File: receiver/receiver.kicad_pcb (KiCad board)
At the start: 2 copper layers, 71.4 x 53.5 mm, 53 parts, among them CON1 AVR-ISP-6, IC1 ATTINY441-SSU, P1 LASER, P2 BATTERY, P3 CONN_01X01, P4 CONN_01X01, P5 CONN_01X01, Q1 OPTO_NPN, Q2 OPTO_NPN, Q3 OPTO_NPN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

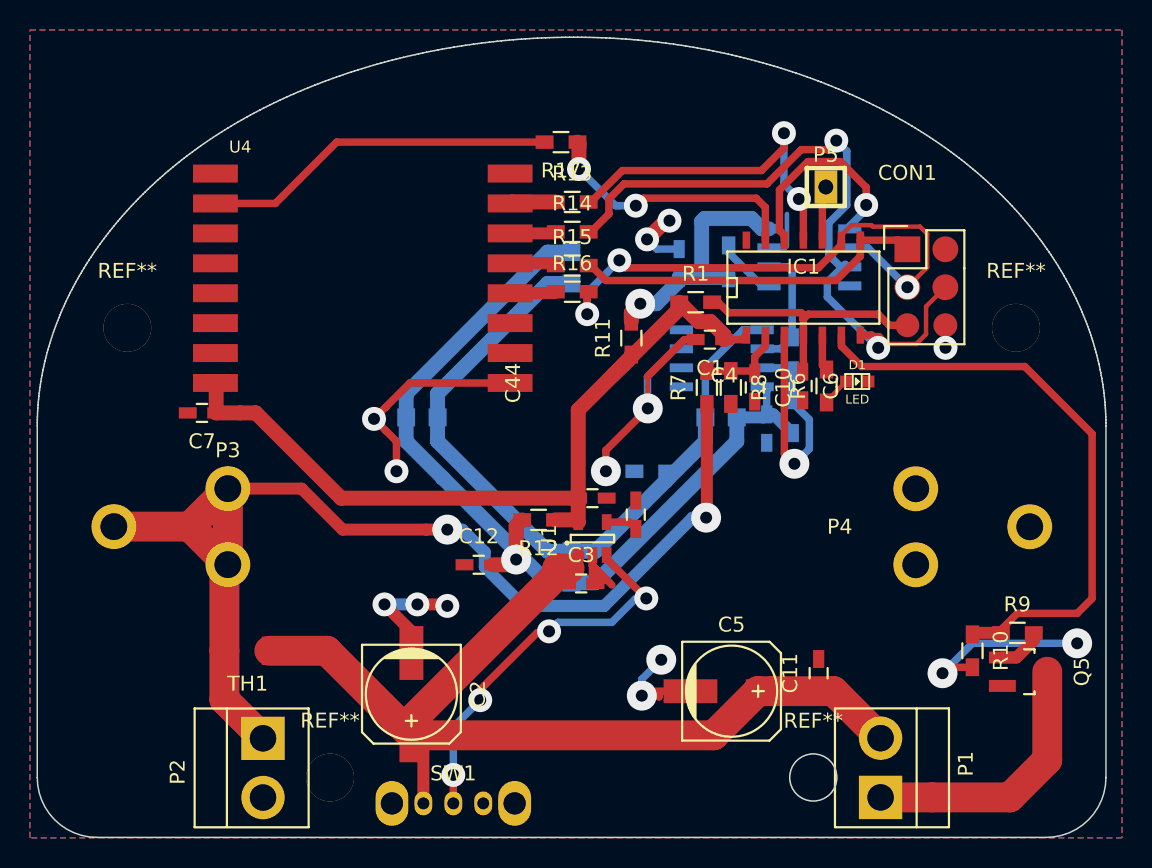
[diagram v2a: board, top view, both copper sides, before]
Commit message: Add connections to the switch on the bottom side
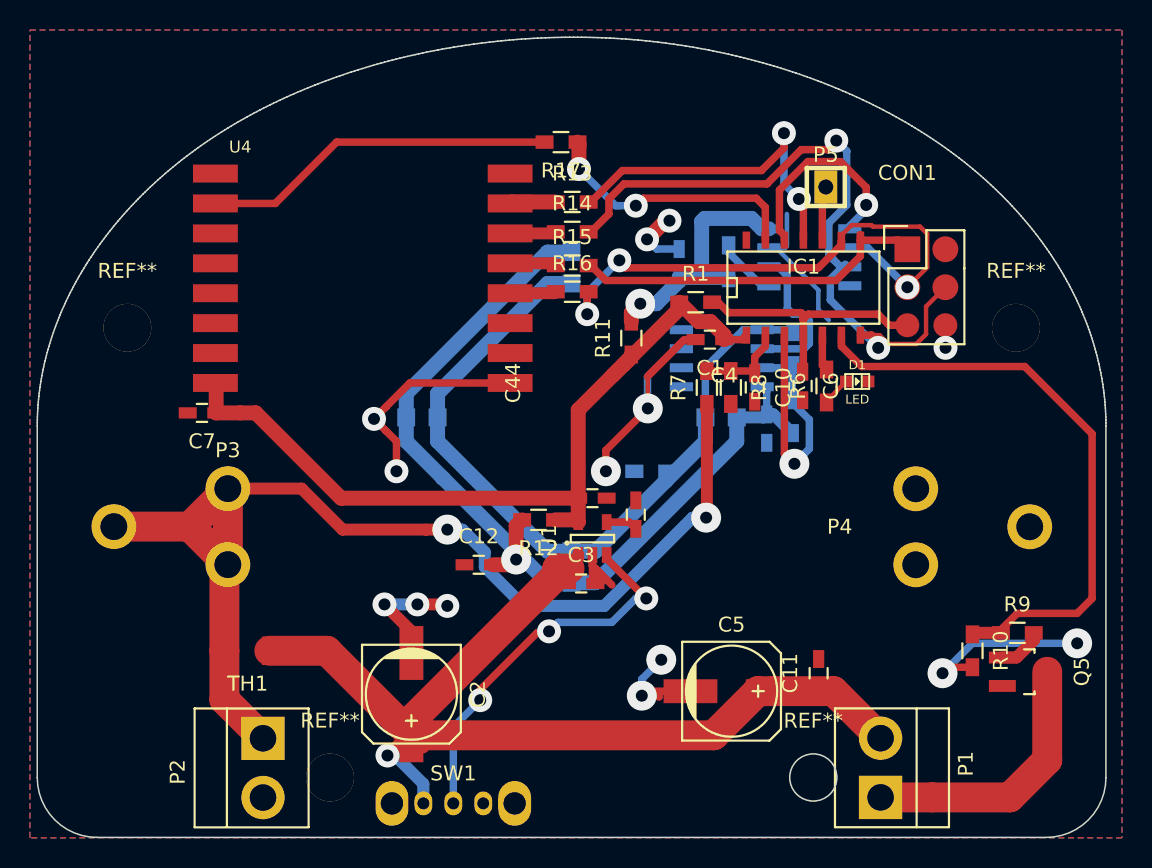
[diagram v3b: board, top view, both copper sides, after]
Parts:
- moved R3 0.35 mm to (102.0, 101.3)
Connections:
- R3 pad 1: /THRESHOLD -> /MATRIX_OUT
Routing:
- net GND: track 76.2 -> 83.0 mm
- net VAA: track 73.1 -> 76.0 mm, vias 0 -> 1
- net /MATRIX_OUT: track 49.7 -> 51.8 mm
- net /THRESHOLD: track 8.51 -> 10.3 mm
- net Net-(SW1-Pad2): vias 4 -> 3
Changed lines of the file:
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@@
     (thickness 1.6)
     (drawings 469)
-    (tracks 393)
+    (tracks 405)
     (zones 0)
     (modules 53)
@@
     (34 B.Paste user hide)
     (35 F.Paste user hide)
-    (36 B.SilkS user hide)
+    (36 B.SilkS user)
     (37 F.SilkS user)
     (38 B.Mask user hide)
@@
   )
   (module Resistors_SMD:R_0603_HandSoldering (layer B.Cu)
-    (at 101.948026 101.65 270)
+    (at 102 101.3 270)
     (descr "Resistor SMD 0603, hand soldering")
     (tags "resistor 0603")
@@
     (fp_line (start -0.5 0.675) (end 0.5 0.675) (layer B.SilkS) (width 0.15))
     (pad 1 smd rect (at -1.1 0 270) (size 1.2 0.9) (layers B.Cu B.Paste B.Mask)
-      (net 16 /THRESHOLD))
+      (net 14 /MATRIX_OUT))
     (pad 2 smd rect (at 1.1 0 270) (size 1.2 0.9) (layers B.Cu B.Paste B.Mask)
       (net 8 /LASER_DETECT))
@@
   (segment (start 63.45 105.6) (end 63.45 103.65) (width 1) (layer F.Cu) (net 1))
   (segment (start 63.45 103.65) (end 63.4 103.6) (width 1) (layer F.Cu) (net 1))
+  (segment (start 103.69999 98.69999) (end 104.4 99.4) (width 0.3) (layer B.Cu) (net 2))
+  (segment (start 100.4 94.565) (end 100.875 94.565) (width 0.3) (layer B.Cu) (net 2))
+  (segment (start 100.875 94.565) (end 103.69999 97.38999) (width 0.3) (layer B.Cu) (net 2))
+  (segment (start 103.69999 97.38999) (end 103.69999 98.69999) (width 0.3) (layer B.Cu) (net 2))
   (segment (start 92.200002 124.2) (end 91.900002 124.5) (width 0.5) (layer F.Cu) (net 2))
   (segment (start 95.14918 124.2) (end 92.200002 124.2) (width 0.5) (layer F.Cu) (net 2))
@@
   (segment (start 95.5 100.7) (end 94.754164 100.7) (width 0.5) (layer F.Cu) (net 2))
   (segment (start 94.754164 100.7) (end 92.277082 103.177082) (width 0.5) (layer F.Cu) (net 2))
+  (segment (start 74.9 128.5) (end 75.4 128.5) (width 0.8) (layer B.Cu) (net 3))
+  (segment (start 75.4 128.5) (end 77.3 130.4) (width 0.8) (layer B.Cu) (net 3))
+  (segment (start 77.3 130.4) (end 77.3 131.7) (width 0.8) (layer B.Cu) (net 3))
+  (segment (start 76.5 127.15082) (end 76.24918 127.15082) (width 0.8) (layer F.Cu) (net 3))
+  (segment (start 76.24918 127.15082) (end 74.9 128.5) (width 0.8) (layer F.Cu) (net 3))
+  (via (at 74.9 128.5) (size 1.6) (drill 0.8) (layers F.Cu B.Cu) (net 3))
   (segment (start 100.65082 124.2) (end 99.65133 124.2) (width 2) (layer F.Cu) (net 3))
   (segment (start 99.65133 124.2) (end 96.70051 127.15082) (width 2) (layer F.Cu) (net 3))
@@
   (segment (start 105.12 124.6) (end 104.72 124.2) (width 2) (layer F.Cu) (net 3))
   (segment (start 104.72 124.2) (end 100.65082 124.2) (width 2) (layer F.Cu) (net 3))
-  (segment (start 77.3 131.7) (end 77.3 127.95082) (width 0.8) (layer F.Cu) (net 3))
   (segment (start 77.3 127.95082) (end 76.5 127.15082) (width 0.8) (layer F.Cu) (net 3))
   (segment (start 79.3001 127.15082) (end 76.5 127.15082) (width 2) (layer F.Cu) (net 3))
@@
   (segment (start 56.61 113.2) (end 61.69 113.2) (width 2) (layer F.Cu) (net 13))
   (segment (start 61.69 113.2) (end 64.23 110.66) (width 2) (layer F.Cu) (net 13))
+  (segment (start 99.948026 100.045) (end 101.845 100.045) (width 0.5) (layer B.Cu) (net 14))
+  (segment (start 101.845 100.045) (end 102 100.2) (width 0.5) (layer B.Cu) (net 14))
   (segment (start 88.79944 114.85098) (end 93.5 110.15042) (width 1) (layer B.Cu) (net 14))
   (segment (start 93.5 110.15042) (end 96.15098 107.49944) (width 1) (layer B.Cu) (net 14))
@@
   (segment (start 116.95 121.95) (end 118.1 120.8) (width 0.8) (layer F.Cu) (net 15))
   (segment (start 118.1 120.8) (end 118.1 120.3) (width 0.8) (layer F.Cu) (net 15))
-  (segment (start 101.948026 100.55) (end 101.183026 101.315) (width 0.5) (layer B.Cu) (net 16))
-  (segment (start 101.183026 101.315) (end 99.948026 101.315) (width 0.5) (layer B.Cu) (net 16))
-  (segment (start 100.4 95.835) (end 101.675 95.835) (width 0.5) (layer B.Cu) (net 16))
-  (segment (start 101.675 95.835) (end 101.948026 96.108026) (width 0.5) (layer B.Cu) (net 16))
-  (segment (start 101.948026 96.108026) (end 101.948026 99.45) (width 0.5) (layer B.Cu) (net 16))
-  (segment (start 101.948026 99.45) (end 101.948026 100.55) (width 0.5) (layer B.Cu) (net 16))
-  (segment (start 102.010705 100.487321) (end 101.948026 100.55) (width 0.3) (layer B.Cu) (net 16))
+  (segment (start 99.948026 101.315) (end 102.745002 101.315) (width 0.5) (layer B.Cu) (net 16))
+  (segment (start 102 99) (end 101.625001 98.625001) (width 0.5) (layer B.Cu) (net 16))
+  (segment (start 102.745002 101.315) (end 103.1 100.960002) (width 0.5) (layer B.Cu) (net 16))
+  (segment (start 103.1 100.960002) (end 103.1 99.439998) (width 0.5) (layer B.Cu) (net 16))
+  (segment (start 103.1 99.439998) (end 102.660002 99) (width 0.5) (layer B.Cu) (net 16))
+  (segment (start 102.660002 99) (end 102 99) (width 0.5) (layer B.Cu) (net 16))
+  (segment (start 101.625001 96.444999) (end 101.015002 95.835) (width 0.5) (layer B.Cu) (net 16))
+  (segment (start 101.625001 98.625001) (end 101.625001 96.444999) (width 0.5) (layer B.Cu) (net 16))
+  (segment (start 101.015002 95.835) (end 100.4 95.835) (width 0.5) (layer B.Cu) (net 16))
   (segment (start 106.51 94.052) (end 106.51 95.1235) (width 0.5) (layer F.Cu) (net 17))
   (segment (start 106.51 95.1235) (end 104.8835 96.75) (width 0.5) (layer F.Cu) (net 17))
@@
   (via (at 109.65 97.2) (size 1.6) (drill 0.8) (layers F.Cu B.Cu) (net 18))
   (segment (start 105.24 94.052) (end 105.24 94.597502) (width 0.5) (layer F.Cu) (net 18))
+  (segment (start 105.325 95.835) (end 104.5 96.66) (width 0.5) (layer B.Cu) (net 19))
+  (segment (start 104.5 96.66) (end 104.5 98.04999) (width 0.5) (layer B.Cu) (net 19))
+  (segment (start 104.5 98.04999) (end 106.700001 100.249991) (width 0.5) (layer B.Cu) (net 19))
+  (segment (start 106.700001 100.249991) (end 107.7 101.24999) (width 0.5) (layer B.Cu) (net 19))
   (segment (start 104.574999 95.225001) (end 104.4 95.050002) (width 0.5) (layer B.Cu) (net 19))
   (segment (start 104.4 95.050002) (end 104.4 92.905037) (width 0.5) (layer B.Cu) (net 19))
@@
   (segment (start 89.7 91.3) (end 90.710036 90.289964) (width 0.5) (layer F.Cu) (net 19))
   (via (at 104.9 87.4) (size 1.6) (drill 0.8) (layers F.Cu B.Cu) (net 19))
-  (segment (start 106.700001 100.249991) (end 107.7 101.24999) (width 0.5) (layer B.Cu) (net 19))
   (segment (start 107.264 100.402) (end 107.7 100.838) (width 0.5) (layer F.Cu) (net 19))
   (via (at 107.7 101.24999) (size 1.6) (drill 0.8) (layers F.Cu B.Cu) (net 19))
-  (segment (start 104.3 97.84999) (end 106.700001 100.249991) (width 0.5) (layer B.Cu) (net 19))
   (segment (start 106.51 100.402) (end 107.264 100.402) (width 0.5) (layer F.Cu) (net 19))
   (segment (start 107.7 100.838) (end 107.7 101.24999) (width 0.5) (layer F.Cu) (net 19))
-  (segment (start 105.325 95.835) (end 104.3 96.86) (width 0.5) (layer B.Cu) (net 19))
-  (segment (start 104.3 96.86) (end 104.3 97.84999) (width 0.5) (layer B.Cu) (net 19))
   (segment (start 105.8 95.835) (end 105.325 95.835) (width 0.5) (layer B.Cu) (net 19))
   (segment (start 112.19 97.2) (end 110.900001 98.489999) (width 0.3) (layer F.Cu) (net 19))
@@
   (segment (start 67.4 91.6) (end 71.5 87.5) (width 0.5) (layer F.Cu) (net 38))
   (segment (start 71.5 87.5) (end 85.4 87.5) (width 0.5) (layer F.Cu) (net 38))
+  (segment (start 79.3 129.8) (end 79.3 131.7) (width 0.5) (layer B.Cu) (net 39))
   (segment (start 92.2 118) (end 91.5 118) (width 0.5) (layer B.Cu) (net 39))
   (segment (start 91.5 118) (end 89.9 119.6) (width 0.5) (layer B.Cu) (net 39))
@@
   (segment (start 84.9 120.3) (end 81.1 124.1) (width 0.5) (layer F.Cu) (net 39))
   (segment (start 81.1 124.1) (end 81.1 124.8) (width 0.5) (layer F.Cu) (net 39))
-  (segment (start 79.3 129.8) (end 79.3 131.7) (width 0.5) (layer F.Cu) (net 39))
   (segment (start 81.1 124.8) (end 79.3 126.6) (width 0.5) (layer B.Cu) (net 39))
   (segment (start 79.3 126.6) (end 79.3 129.8) (width 0.5) (layer B.Cu) (net 39))
-  (via (at 79.3 129.8) (size 1.6) (drill 0.8) (layers F.Cu B.Cu) (net 39))
   (via (at 81.1 124.8) (size 1.6) (drill 0.8) (layers F.Cu B.Cu) (net 39))
   (via (at 85.7 120.2) (size 1.6) (drill 0.8) (layers F.Cu B.Cu) (net 39))
